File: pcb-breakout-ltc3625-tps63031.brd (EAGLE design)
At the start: 40 x 22.7 mm, 16 parts, among them IC1 LTC3625EDE

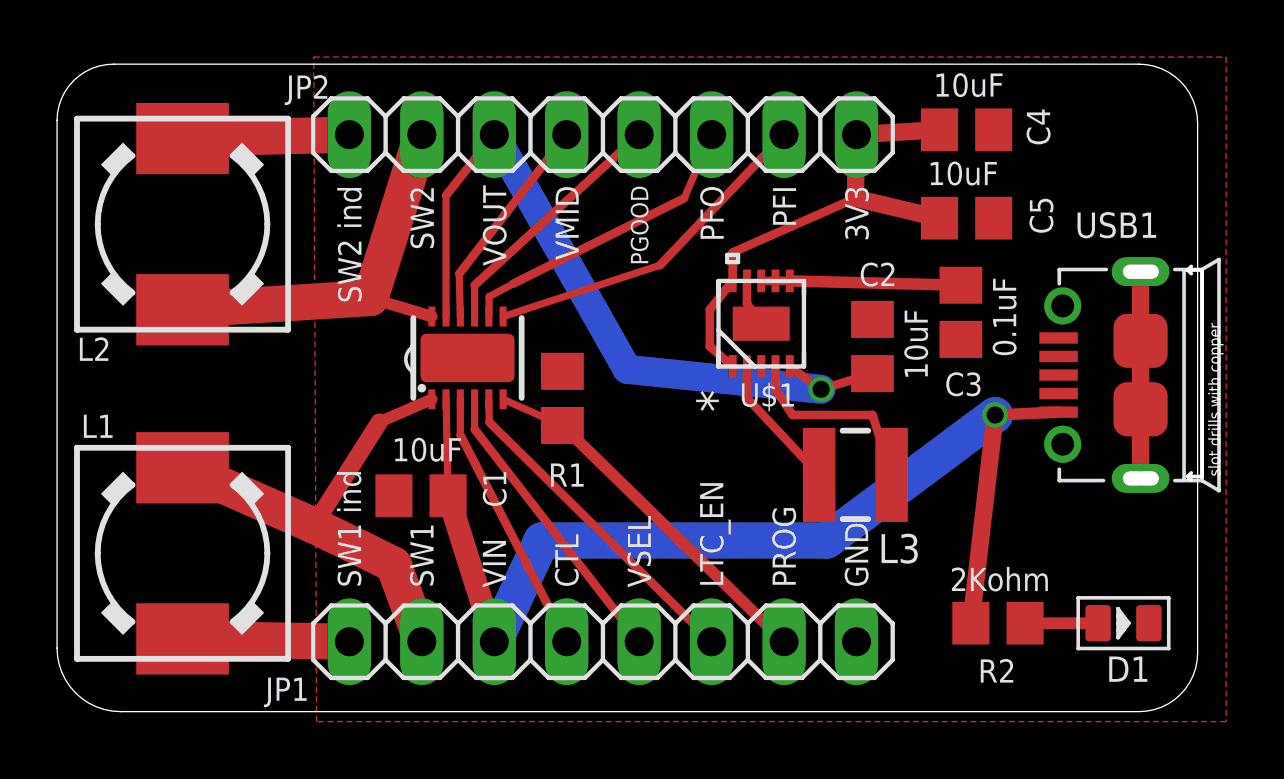
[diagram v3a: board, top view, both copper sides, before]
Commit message: Breakout pins TPS EN and PS and add pull up resistors to them
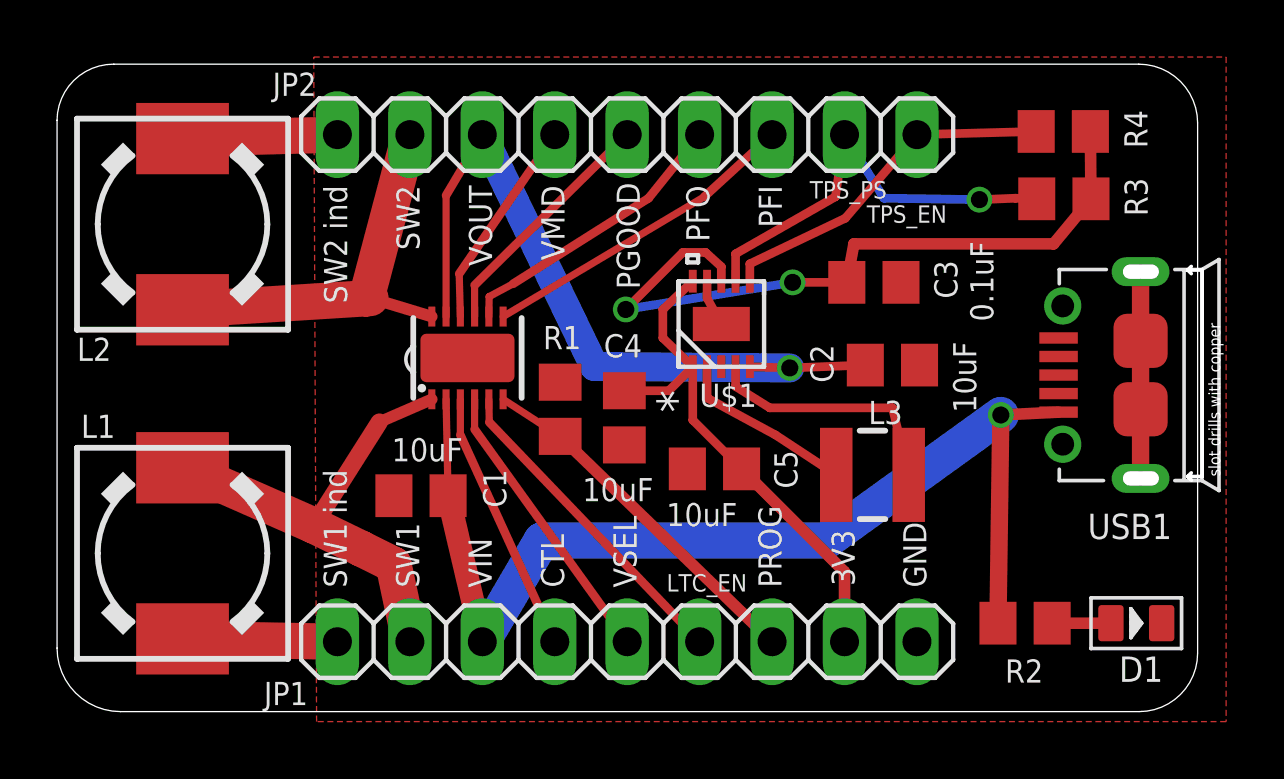
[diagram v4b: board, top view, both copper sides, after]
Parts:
- added R3, R4: 10kohm, resistor:R0805
- JP1, JP2: device pinhead:1X08 -> pinhead:1X09
- R2: value 2Kohm -> 2kohm
- moved C4 15.7 mm to (19.9, 10.3), turned to 270 degrees
- moved C5 12.5 mm to (23.1, 8.51), turned to 180 degrees
- moved C3 3.23 mm to (28.6, 15.1), turned to 0 degrees
- moved U$1 1.40 mm to (23.3, 13.6)
- moved C2 0.96 mm to (29.3, 12.2), turned to 0 degrees
- moved R2 0.95 mm to (34.0, 3.10)
- moved JP1 0.85 mm to (20.0, 2.45)
- moved JP2 0.85 mm to (20.0, 20.2)
- moved L3 0.60 mm to (28.6, 8.30)
- moved D1 0.45 mm to (37.9, 3.10)
- moved R1 0.39 mm to (17.6, 10.6)
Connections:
- new net TPS63031_EN: JP2.1, R4.1, U$1.6
- new net TPS63031_PS: JP2.2, R3.1, U$1.7
- net GND: now also JP1.9; no longer JP1.8
- net L3625_PFI: now also JP2.3; no longer JP2.2
- net L3625_PFO: now also JP2.4; no longer JP2.3
- net L3625_PGOOD: now also JP2.5; no longer JP2.4
- net L3625_SW2: now also JP2.8; no longer JP2.7
- net L3625_SW2_IND: now also JP2.9; no longer JP2.8
- net L3625_VMID: now also JP2.6; no longer JP2.5
- net L3625_VOUT: now also JP2.7; no longer JP2.6
- net N$5: now also R3.2, R4.2; no longer U$1.6, U$1.7
- net TPS63031_VOUT: now also JP1.8; no longer JP2.1
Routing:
- net N$5: track 7.00 -> 25.5 mm, vias 0 -> 2
- net TPS63031_PS: track 0.00 -> 15.2 mm, vias 0 -> 1
- net TPS63031_EN: track 0.00 -> 12.4 mm
- net N$2: track 6.89 -> 8.82 mm
- net N$1: track 4.80 -> 6.37 mm
- net TPS63031_VOUT: track 17.5 -> 18.5 mm
- net L3625_PFI: track 12.1 -> 11.4 mm
- net L3625_PFO: track 10.8 -> 10.1 mm
- net N$3: track 2.56 -> 2.06 mm
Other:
- board text added: "TPS_EN"
- board text added: "TPS_PS"
